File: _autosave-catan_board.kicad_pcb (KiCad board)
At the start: 2 copper layers, 58 parts

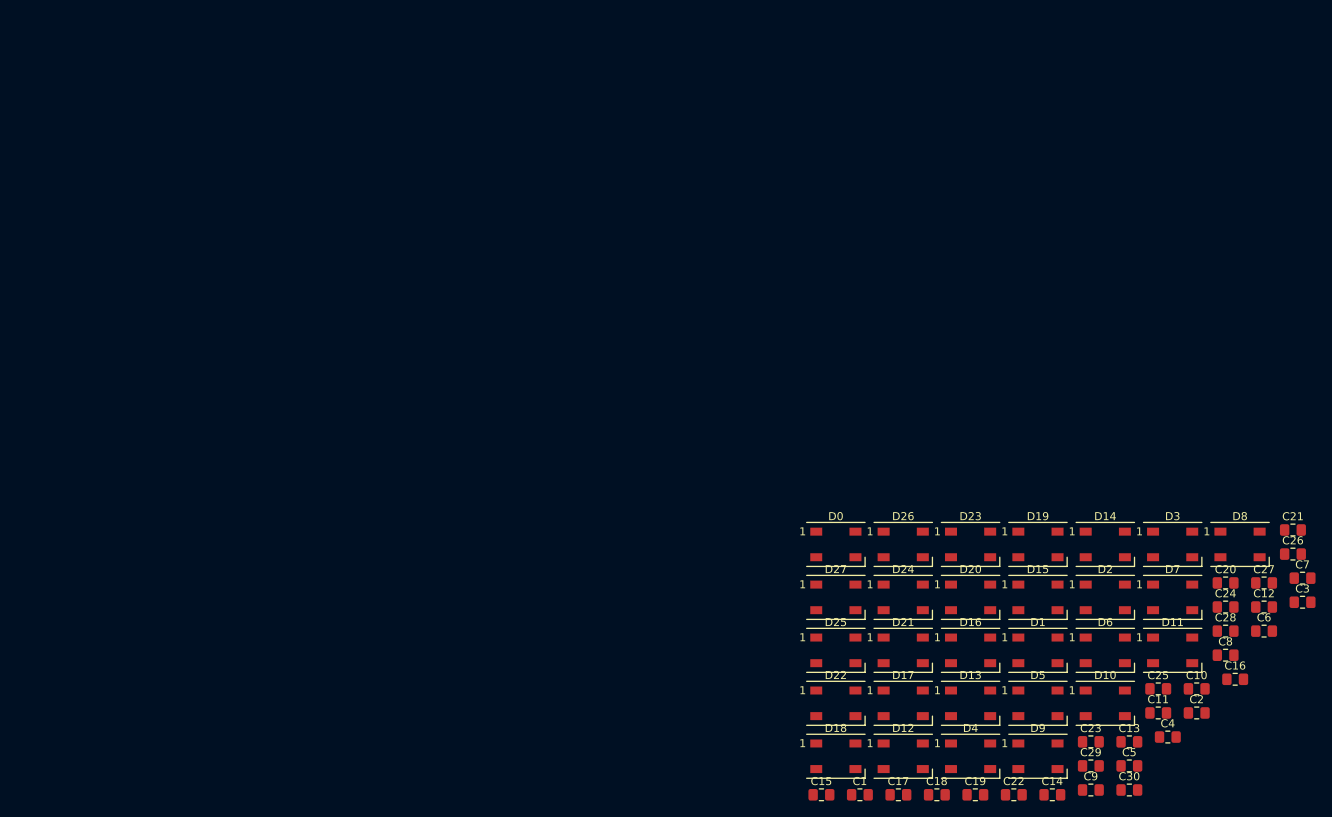
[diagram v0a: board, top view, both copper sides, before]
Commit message: gnd pour done, maybe should add 5v rail on other side
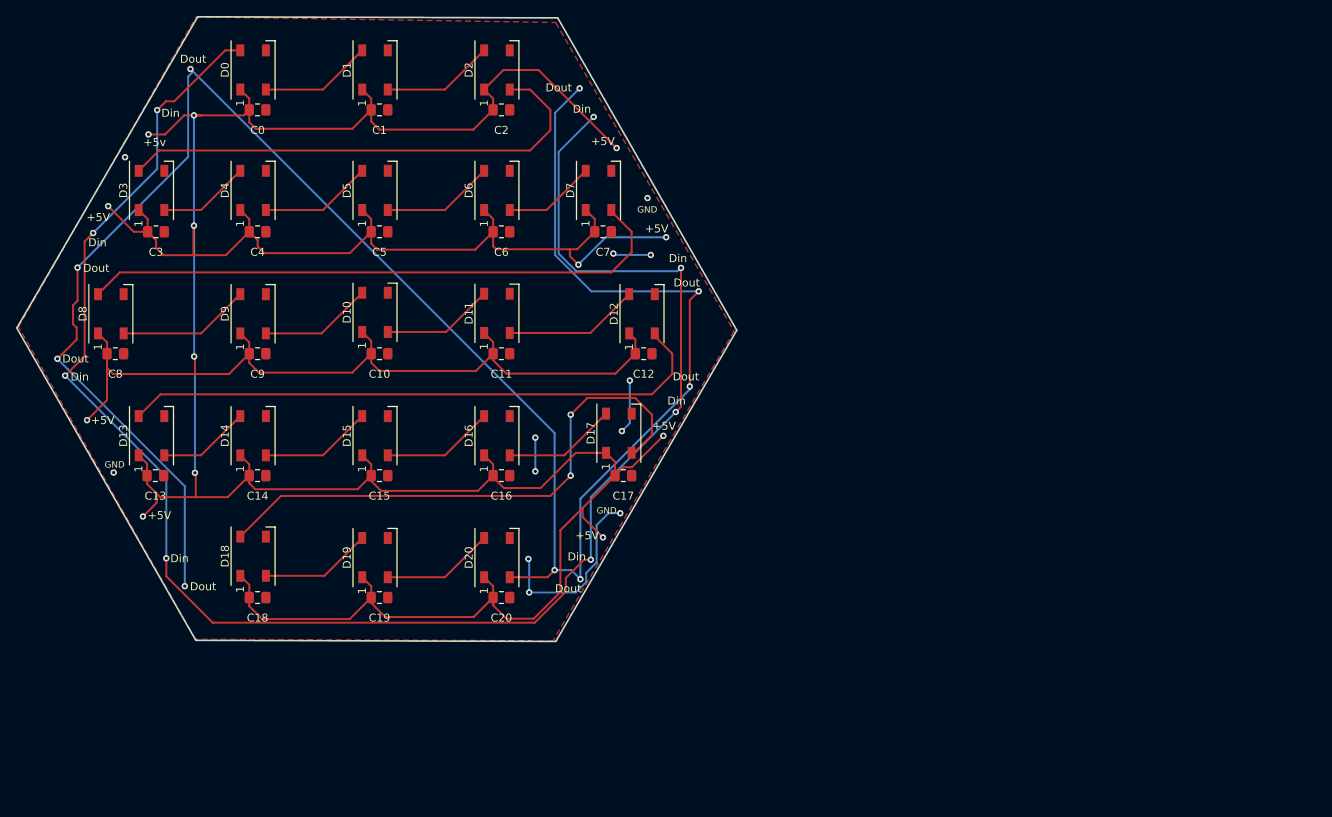
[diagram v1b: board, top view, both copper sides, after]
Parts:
- removed the C12 at (249.2, 128.2)
- removed the C14 at (222.8, 151.7)
- removed C22, C23, C24, C25, C27, C28, C29: C_Small, Capacitor_SMD:C_0805_2012Metric_Pad1.18x1.45mm_HandSolder
- removed D21, D22, D23, D24, D25, D26, D27: WS2812B, LED_SMD:LED_WS2812B_PLCC4_5.0x5.0mm_P3.2mm
- moved C3 150.6 mm to (110.7, 81.3)
- moved D8 144.1 mm to (105.1, 91.5), turned to 90 degrees
- moved C8 143.8 mm to (105.6, 96.5)
- moved C0 138.2 mm to (123.4, 66.0)
- moved D3 135.1 mm to (110.2, 76.1), turned to 90 degrees
- moved C4 130.1 mm to (123.4, 81.3)
- moved C14 129.8 mm to (123.4, 111.8)
- moved C13 126.2 mm to (110.6, 111.8)
- moved C9 117.6 mm to (123.4, 96.5)
- moved C5 115.1 mm to (138.7, 81.3)
- moved C2 115.1 mm to (153.9, 66.0)
- moved D4 114.2 mm to (122.9, 76.1), turned to 90 degrees
- moved D9 112.6 mm to (122.9, 91.5), turned to 90 degrees
- moved C10 110.4 mm to (138.7, 96.5)
- moved D1 110.1 mm to (138.1, 61.0), turned to 90 degrees
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- renumbered C30 to C0, C21 to C12, C26 to C14
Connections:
- D14 pad 1: 5V -> +5V
- D15 pad 1: 5V -> +5V
- D16 pad 1: 5V -> +5V
- D17 pad 1: 5V -> +5V
- D18 pad 1: 5V -> +5V
- D19 pad 1: 5V -> +5V
- D20 pad 1: 5V -> +5V
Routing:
- net +5V: track 0.00 -> 514.0 mm, vias 0 -> 13
- net Net-(D20-Pad2): track 0.00 -> 253.5 mm, vias 0 -> 9
- net Net-(D0-Pad4): track 0.00 -> 217.9 mm, vias 0 -> 8
- net Net-(D7-Pad2): track 0.00 -> 75.2 mm
- net Net-(D12-Pad2): track 0.00 -> 74.9 mm
- net Net-(D17-Pad2): track 0.00 -> 70.0 mm, vias 0 -> 2
- net Net-(D2-Pad2): track 0.00 -> 62.2 mm
- net GND: track 0.00 -> 38.8 mm, vias 0 -> 12
- net Net-(D11-Pad2): track 0.00 -> 16.9 mm
- net Net-(D8-Pad2): track 0.00 -> 16.6 mm
- net Net-(D16-Pad2): track 0.00 -> 14.2 mm
- net Net-(D10-Pad4): track 0.00 -> 14.1 mm
- net Net-(D5-Pad2): track 0.00 -> 14.1 mm
- net Net-(D15-Pad2): track 0.00 -> 14.1 mm
- net Net-(D1-Pad2): track 0.00 -> 14.1 mm
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- added copper zone on F.Cu, net GND
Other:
- board outline added: 90 x 78.1 mm
- board text added: "+5V"
- board text added: "+5v"
- board text added: "Din"
- board text added: "Dout"
- board text added: "GND"
